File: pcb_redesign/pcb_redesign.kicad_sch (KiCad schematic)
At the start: 6 parts, among them U1 ESP32-S3-WROOM-1

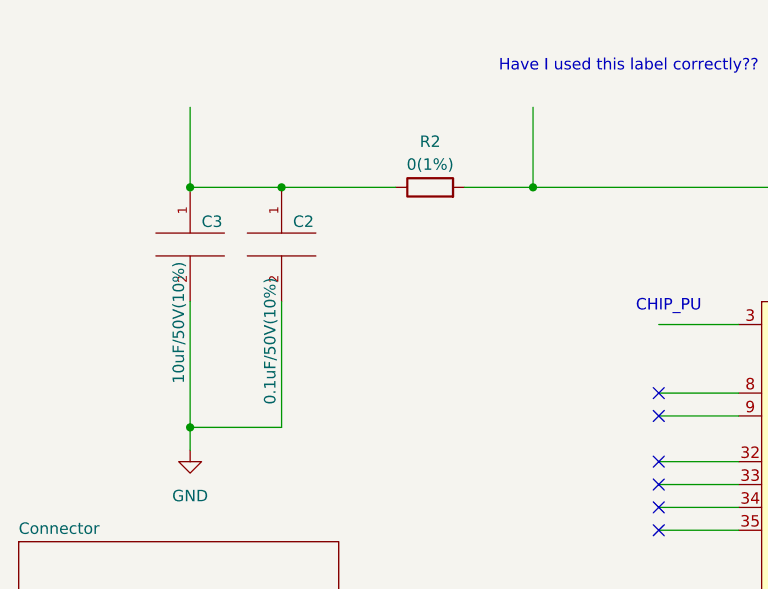
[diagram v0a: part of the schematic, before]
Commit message: schematic imported
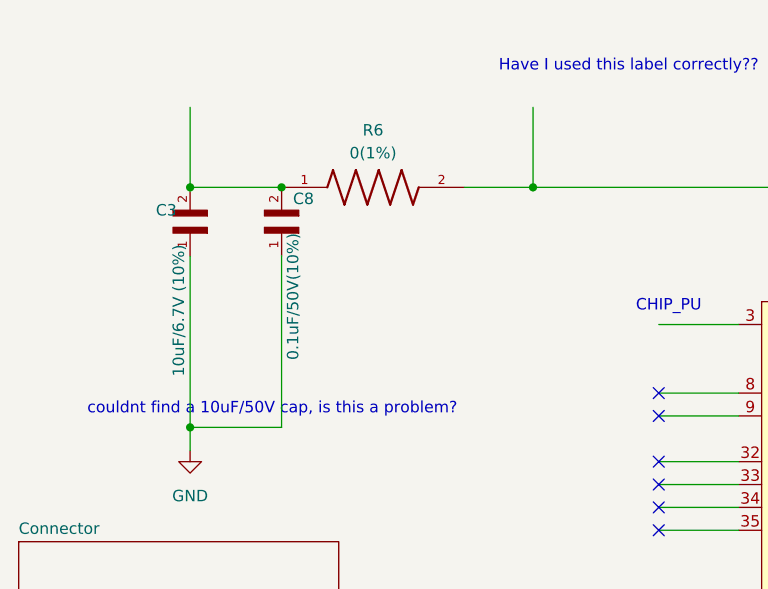
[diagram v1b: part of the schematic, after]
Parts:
- removed C2: 0.1uF/50V(10%), symbol pspice:C
- removed C3: 10uF/50V(10%), 10uF_cap_0805:CAPC2012X140N, symbol pspice:C
- removed R2: 0(1%), symbol Device:R
- added C3: 10uF/6.7V (10%), CAPC1608X90N, symbol 10uf_cap_0603:CL10A106MQ8NNNC
- added C8: 0.1uF/50V(10%), 1uF_cap_0603:CL10A105KB8NNNC, symbol 0.1uF_cap_0603:CL10B104KB8NNNL
- added R6: 0(1%), RESC1508X55N, symbol 0_ohm_0603:RMCF0603ZT0R00
- C1: footprint (none) -> 1uF_cap_0603:CL10A105KB8NNNC
- R1: footprint (none) -> 10k_ohm_0603:RESC1508X50N
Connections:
- net GND: now also C3.1, C8.1
- net at U1.2 (3V3): now also R6.2
- new net: C3.2, C8.2, R6.1
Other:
- note added: "couldnt find a 10uF/50V cap, is this a problem?"
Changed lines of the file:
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@@
 (kicad_sch (version 20230121) (generator eeschema)
   (paper "A4")
+  (junction (at 46.99 43.18) (diameter 0) (color 0 0 0 0)
+  )
   (junction (at 36.83 43.18) (diameter 0) (color 0 0 0 0)
   )
   (junction (at 36.83 69.85) (diameter 0) (color 0 0 0 0)
-  )
-  (junction (at 46.99 43.18) (diameter 0) (color 0 0 0 0)
   )
   (junction (at 66.04 175.26) (diameter 0) (color 0 0 0 0)
@@
     (stroke (width 0) (type default))
   )
+  (wire (pts (xy 88.9 129.54) (xy 97.79 129.54))
+    (stroke (width 0) (type default))
+  )
+  (wire (pts (xy 88.9 81.28) (xy 97.79 81.28))
+    (stroke (width 0) (type default))
+  )
+  (wire (pts (xy 88.9 68.58) (xy 97.79 68.58))
+    (stroke (width 0) (type default))
+  )
+  (wire (pts (xy 36.83 69.85) (xy 46.99 69.85))
+    (stroke (width 0) (type default))
+  )
+  (wire (pts (xy 189.23 129.54) (xy 199.39 129.54))
+    (stroke (width 0) (type default))
+  )
+  (wire (pts (xy 189.23 119.38) (xy 199.39 119.38))
+    (stroke (width 0) (type default))
+  )
   (wire (pts (xy 36.83 43.18) (xy 46.99 43.18))
     (stroke (width 0) (type default))
   )
-  (wire (pts (xy 88.9 129.54) (xy 97.79 129.54))
-    (stroke (width 0) (type default))
-  )
-  (wire (pts (xy 88.9 81.28) (xy 97.79 81.28))
-    (stroke (width 0) (type default))
-  )
-  (wire (pts (xy 88.9 68.58) (xy 97.79 68.58))
-    (stroke (width 0) (type default))
-  )
-  (wire (pts (xy 36.83 69.85) (xy 46.99 69.85))
-    (stroke (width 0) (type default))
-  )
-  (wire (pts (xy 189.23 129.54) (xy 199.39 129.54))
-    (stroke (width 0) (type default))
-  )
-  (wire (pts (xy 189.23 119.38) (xy 199.39 119.38))
-    (stroke (width 0) (type default))
-  )
   (wire (pts (xy 189.23 99.06) (xy 199.39 99.06))
     (stroke (width 0) (type default))
@@
     (stroke (width 0) (type default))
   )
-  (wire (pts (xy 46.99 43.18) (xy 59.69 43.18))
-    (stroke (width 0) (type default))
-  )
   (wire (pts (xy 36.83 69.85) (xy 36.83 72.39))
     (stroke (width 0) (type default))
@@
     (stroke (width 0) (type default))
   )
-  (wire (pts (xy 36.83 55.88) (xy 36.83 69.85))
+  (wire (pts (xy 36.83 50.8) (xy 36.83 69.85))
     (stroke (width 0) (type default))
   )
@@
     (stroke (width 0) (type default))
   )
-  (wire (pts (xy 46.99 55.88) (xy 46.99 69.85))
+  (wire (pts (xy 46.99 50.8) (xy 46.99 69.85))
     (stroke (width 0) (type default))
   )
@@
   )
   (text "Have I used this label correctly??" (at 71.12 30.48 0)
+    (effects (font (size 1.27 1.27)) (justify left bottom))
+  )
+  (text "couldnt find a 10uF/50V cap, is this a problem?" (at 25.4 68.58 0)
     (effects (font (size 1.27 1.27)) (justify left bottom))
   )
@@
       (effects (font (size 1.27 1.27)) (justify left))
     )
-    (property "Footprint" "" (at 64.262 168.91 90)
+    (property "Footprint" "10k_ohm_0603:RESC1508X50N" (at 64.262 168.91 90)
       (effects (font (size 1.27 1.27)) hide)
     )
@@
     )
   )
-  (symbol (lib_id "pspice:C") (at 46.99 49.53 0) (unit 1)
+  (symbol (lib_id "10uf_cap_0603:CL10A106MQ8NNNC") (at 36.83 48.26 90) (unit 1)
     (in_bom yes) (on_board yes) (dnp no)
-    (property "Reference" "C2" (at 48.26 46.99 0)
-      (effects (font (size 1.27 1.27)) (justify left))
-    )
-    (property "Value" "0.1uF/50V(10%)" (at 45.72 67.31 90)
-      (effects (font (size 1.27 1.27)) (justify left))
-    )
-    (property "Footprint" "" (at 46.99 49.53 0)
-      (effects (font (size 1.27 1.27)) hide)
-    )
-    (property "Datasheet" "~" (at 46.99 49.53 0)
+    (property "Reference" "C3" (at 33.02 45.72 90)
+      (effects (font (size 1.27 1.27)) (justify right))
+    )
+    (property "Value" "10uF/6.7V (10%)" (at 35.56 49.53 0)
+      (effects (font (size 1.27 1.27)) (justify right))
+    )
+    (property "Footprint" "CAPC1608X90N" (at 36.83 48.26 0)
+      (effects (font (size 1.27 1.27)) (justify bottom) hide)
+    )
+    (property "Datasheet" "" (at 36.83 48.26 0)
       (effects (font (size 1.27 1.27)) hide)
     )
@@
       (project "pcb_redesign"
         (path "/fb030e39-7dd3-46a0-8379-c26b3ef1b0a0"
-          (reference "C2") (unit 1)
-        )
-      )
-    )
-  )
-  (symbol (lib_id "Device:R") (at 63.5 43.18 90) (unit 1)
-    (in_bom yes) (on_board yes) (dnp no) (fields_autoplaced)
-    (property "Reference" "R2" (at 63.5 38.1 90)
-      (effects (font (size 1.27 1.27)))
-    )
-    (property "Value" "0(1%)" (at 63.5 40.64 90)
-      (effects (font (size 1.27 1.27)))
-    )
-    (property "Footprint" "" (at 63.5 44.958 90)
-      (effects (font (size 1.27 1.27)) hide)
-    )
-    (property "Datasheet" "~" (at 63.5 43.18 0)
+          (reference "C3") (unit 1)
+        )
+      )
+    )
+  )
+  (symbol (lib_id "0.1uF_cap_0603:CL10B104KB8NNNL") (at 46.99 48.26 90) (unit 1)
+    (in_bom yes) (on_board yes) (dnp no)
+    (property "Reference" "C8" (at 48.26 44.45 90)
+      (effects (font (size 1.27 1.27)) (justify right))
+    )
+    (property "Value" "0.1uF/50V(10%)" (at 48.26 48.26 0)
+      (effects (font (size 1.27 1.27)) (justify right))
+    )
+    (property "Footprint" "1uF_cap_0603:CL10A105KB8NNNC" (at 46.99 48.26 0)
+      (effects (font (size 1.27 1.27)) (justify bottom) hide)
+    )
+    (property "Datasheet" "" (at 46.99 48.26 0)
       (effects (font (size 1.27 1.27)) hide)
     )
@@
       (project "pcb_redesign"
         (path "/fb030e39-7dd3-46a0-8379-c26b3ef1b0a0"
-          (reference "R2") (unit 1)
+          (reference "C8") (unit 1)
         )
       )
@@
         (path "/fb030e39-7dd3-46a0-8379-c26b3ef1b0a0"
           (reference "#PWR01") (unit 1)
-        )
-      )
-    )
-  )
-  (symbol (lib_id "pspice:C") (at 36.83 49.53 0) (unit 1)
-    (in_bom yes) (on_board yes) (dnp no)
-    (property "Reference" "C3" (at 38.1 46.99 0)
-      (effects (font (size 1.27 1.27)) (justify left))
-    )
-    (property "Value" "10uF/50V(10%)" (at 35.56 51.435 90)
-      (effects (font (size 1.27 1.27)) (justify right))
-    )
-    (property "Footprint" "10uF_cap_0805:CAPC2012X140N" (at 36.83 49.53 0)
-      (effects (font (size 1.27 1.27)) hide)
-    )
-    (property "Datasheet" "~" (at 36.83 49.53 0)
-      (effects (font (size 1.27 1.27)) hide)
-    )
-    (pin "1")
-    (pin "2")
-    (instances
-      (project "pcb_redesign"
-        (path "/fb030e39-7dd3-46a0-8379-c26b3ef1b0a0"
-          (reference "C3") (unit 1)
         )
       )
@@
       (effects (font (size 1.27 1.27)) (justify left))
     )
-    (property "Footprint" "" (at 66.04 184.15 0)
+    (property "Footprint" "1uF_cap_0603:CL10A105KB8NNNC" (at 66.04 184.15 0)
       (effects (font (size 1.27 1.27)) hide)
     )
@@
         )
       )
+    )
+  )
+  (symbol (lib_id "0_ohm_0603:RMCF0603ZT0R00") (at 57.15 43.18 0) (unit 1)
+    (in_bom yes) (on_board yes) (dnp no) (fields_autoplaced)
+    (property "Reference" "R6" (at 57.15 36.83 0)
+      (effects (font (size 1.27 1.27)))
+    )
+    (property "Value" "0(1%)" (at 57.15 39.37 0)
+      (effects (font (size 1.27 1.27)))
+    )
+    (property "Footprint" "RESC1508X55N" (at 57.15 43.18 0)
+      (effects (font (size 1.27 1.27)) (justify bottom) hide)
+    )
+    (property "Datasheet" "" (at 57.15 43.18 0)
+      (effects (font (size 1.27 1.27)) hide)
+    )
+    (pin "1")
+    (pin "2")
+    (instances
+      (project "pcb_redesign"
+        (path "/fb030e39-7dd3-46a0-8379-c26b3ef1b0a0"
+          (reference "R6") (unit 1)
+        )
+      )

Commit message: components added to board
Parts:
- added JP1: SolderJumper_2_Open, Jumper:SolderJumper-2_P1.3mm_Open_Pad1.0x1.5mm, symbol Jumper:SolderJumper_2_Open
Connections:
- net ESP32_3V3: now reaches R1.1
- net ESP32_3V3: now also R6.2, U1.2 (3V3)
- net CHIP_PU: now reaches C1.1, R1.2
- net CHIP_PU: now also U1.3 (EN)
- net VCC_3V3: now reaches C3.2, C8.2, R6.1
- net at U1.10 (GPIO17/U1TXD/ADC2_CH6): now also JP1.2 (B)
- net at U1.11 (GPIO18/U1RXD/ADC2_CH7/CLK_OUT3): now also JP1.1 (A)
- no-connect marks 30 -> 28
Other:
- note removed: "CHIP_PU"
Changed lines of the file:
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@@
   (no_connect (at 88.9 81.28))
   (no_connect (at 199.39 124.46))
-  (no_connect (at 199.39 114.3))
-  (no_connect (at 199.39 111.76))
   (no_connect (at 199.39 106.68))
   (no_connect (at 199.39 58.42))
@@
     (stroke (width 0) (type default))
   )
+  (wire (pts (xy 203.2 114.3) (xy 203.2 116.84))
+    (stroke (width 0) (type default))
+  )
   (wire (pts (xy 36.83 69.85) (xy 36.83 72.39))
     (stroke (width 0) (type default))
   )
-  (wire (pts (xy 189.23 114.3) (xy 199.39 114.3))
+  (wire (pts (xy 189.23 114.3) (xy 203.2 114.3))
     (stroke (width 0) (type default))
   )
@@
     (stroke (width 0) (type default))
   )
+  (wire (pts (xy 189.23 111.76) (xy 203.2 111.76))
+    (stroke (width 0) (type default))
+  )
   (wire (pts (xy 67.31 43.18) (xy 74.93 43.18))
     (stroke (width 0) (type default))
@@
     (stroke (width 0) (type default))
   )
-  (wire (pts (xy 189.23 111.76) (xy 199.39 111.76))
+  (wire (pts (xy 203.2 111.76) (xy 203.2 109.22))
     (stroke (width 0) (type default))
   )
@@
     (stroke (width 0) (type default))
   )
+  (wire (pts (xy 203.2 116.84) (xy 207.01 116.84))
+    (stroke (width 0) (type default))
+  )
   (wire (pts (xy 189.23 104.14) (xy 199.39 104.14))
     (stroke (width 0) (type default))
@@
     (stroke (width 0) (type default))
   )
+  (wire (pts (xy 203.2 109.22) (xy 207.01 109.22))
+    (stroke (width 0) (type default))
+  )
   (wire (pts (xy 189.23 81.28) (xy 199.39 81.28))
     (stroke (width 0) (type default))
@@
     (stroke (width 0) (type default))
   )
-  (text "Goes to pad (and then gnd..?)" (at 208.28 115.57 0)
+  (text "Goes to pad (and then gnd..?)" (at 232.41 106.68 0)
     (effects (font (size 1.27 1.27)) (justify left bottom))
   )
@@
     (effects (font (size 1.27 1.27)) (justify left bottom))
   )
-  (text "Goes to pad (and then gnd..?)" (at 208.28 113.03 0)
+  (text "Goes to pad (and then gnd..?)" (at 232.41 104.14 0)
     (effects (font (size 1.27 1.27)) (justify left bottom))
   )
@@
     (effects (font (size 1.27 1.27)) (justify left bottom))
   )
-  (text "CHIP_PU" (at 74.93 175.26 0)
-    (effects (font (size 1.27 1.27)) (justify left bottom))
-  )
   (text "If I dont want a pin to be accessible, do I ground the pin or do I mark it as not connected\nAnswer: mark as nc"
     (at 193.04 50.8 0)
     (effects (font (size 1.27 1.27)) (justify left bottom))
   )
-  (text "CHIP_PU" (at 86.36 57.15 0)
-    (effects (font (size 1.27 1.27)) (justify left bottom))
+  (label "CHIP_PU" (at 78.74 175.26 0) (fields_autoplaced)
+    (effects (font (size 1.27 1.27)) (justify left bottom))
+  )
+  (label "CHIP_PU" (at 88.9 58.42 0) (fields_autoplaced)
+    (effects (font (size 1.27 1.27)) (justify left bottom))
+  )
+  (label "ESP32_3V3" (at 66.04 165.1 0) (fields_autoplaced)
+    (effects (font (size 1.27 1.27)) (justify left bottom))
+  )
+  (label "ESP32_3V3" (at 74.93 34.29 0) (fields_autoplaced)
+    (effects (font (size 1.27 1.27)) (justify left bottom))
+  )
+  (global_label "GND" (shape output) (at 143.51 134.62 270) (fields_autoplaced)
+    (effects (font (size 1.27 1.27)) (justify right))
+    (property "Intersheetrefs" "${INTERSHEET_REFS}" (at 143.51 141.3963 90)
+      (effects (font (size 1.27 1.27)) (justify right) hide)
+    )
   )
   (global_label "ENB Left Motor" (shape output) (at 199.39 86.36 0) (fields_autoplaced)
@@
     )
   )
+  (global_label "VCC_3V3" (shape input) (at 36.83 34.29 90) (fields_autoplaced)
+    (effects (font (size 1.27 1.27)) (justify left))
+    (property "Intersheetrefs" "${INTERSHEET_REFS}" (at 36.83 23.2804 90)
+      (effects (font (size 1.27 1.27)) (justify left) hide)
+    )
+  )
   (global_label "D-" (shape input) (at 199.39 68.58 0) (fields_autoplaced)
     (effects (font (size 1.27 1.27)) (justify left))
@@
     )
   )
+  (global_label "GND" (shape output) (at 66.04 190.5 270) (fields_autoplaced)
+    (effects (font (size 1.27 1.27)) (justify right))
+    (property "Intersheetrefs" "${INTERSHEET_REFS}" (at 66.04 197.2763 90)
+      (effects (font (size 1.27 1.27)) (justify right) hide)
+    )
+  )
+  (global_label "GND" (shape output) (at 36.83 72.39 270) (fields_autoplaced)
+    (effects (font (size 1.27 1.27)) (justify right))
+    (property "Intersheetrefs" "${INTERSHEET_REFS}" (at 36.83 79.1663 90)
+      (effects (font (size 1.27 1.27)) (justify right) hide)
+    )
+  )
   (global_label "D+" (shape input) (at 199.39 66.04 0) (fields_autoplaced)
     (effects (font (size 1.27 1.27)) (justify left))
     (property "Intersheetrefs" "${INTERSHEET_REFS}" (at 205.1382 66.04 0)
       (effects (font (size 1.27 1.27)) (justify left) hide)
-    )
-  )
-  (netclass_flag "" (length 2.54) (shape round) (at 66.04 165.1 0) (fields_autoplaced)
-    (effects (font (size 1.27 1.27)) (justify left bottom))
-    (property "Netclass" "ESP32_3V3" (at 66.7385 162.56 0)
-      (effects (font (size 1.27 1.27) italic) (justify left))
-    )
-  )
-  (netclass_flag "" (length 2.54) (shape round) (at 36.83 34.29 0) (fields_autoplaced)
-    (effects (font (size 1.27 1.27)) (justify left bottom))
-    (property "Netclass" "VCC_3V3" (at 37.5285 31.75 0)
-      (effects (font (size 1.27 1.27) italic) (justify left))
-    )
-  )
-  (netclass_flag "" (length 2.54) (shape round) (at 74.93 34.29 0) (fields_autoplaced)
-    (effects (font (size 1.27 1.27)) (justify left bottom))
-    (property "Netclass" "ESP32_3V3" (at 75.6285 31.75 0)
-      (effects (font (size 1.27 1.27) italic) (justify left))
     )
   )
@@
         (path "/fb030e39-7dd3-46a0-8379-c26b3ef1b0a0"
           (reference "C8") (unit 1)
-        )
-      )
-    )
-  )
-  (symbol (lib_id "power:GND") (at 143.51 134.62 0) (unit 1)
-    (in_bom yes) (on_board yes) (dnp no) (fields_autoplaced)
-    (property "Reference" "#PWR01" (at 143.51 140.97 0)
-      (effects (font (size 1.27 1.27)) hide)
-    )
-    (property "Value" "GND" (at 143.51 139.7 0)
-      (effects (font (size 1.27 1.27)))
-    )
-    (property "Footprint" "" (at 143.51 134.62 0)
-      (effects (font (size 1.27 1.27)) hide)
-    )
-    (property "Datasheet" "" (at 143.51 134.62 0)
-      (effects (font (size 1.27 1.27)) hide)
-    )
-    (pin "1")
-    (instances
-      (project "pcb_redesign"
-        (path "/fb030e39-7dd3-46a0-8379-c26b3ef1b0a0"
-          (reference "#PWR01") (unit 1)
-        )
-      )
-    )
-  )
-  (symbol (lib_id "power:GND") (at 66.04 190.5 0) (unit 1)
-    (in_bom yes) (on_board yes) (dnp no) (fields_autoplaced)
-    (property "Reference" "#PWR02" (at 66.04 196.85 0)
-      (effects (font (size 1.27 1.27)) hide)
-    )
-    (property "Value" "GND" (at 66.04 195.58 0)
-      (effects (font (size 1.27 1.27)))
-    )
-    (property "Footprint" "" (at 66.04 190.5 0)
-      (effects (font (size 1.27 1.27)) hide)
-    )
-    (property "Datasheet" "" (at 66.04 190.5 0)
-      (effects (font (size 1.27 1.27)) hide)
-    )
-    (pin "1")
-    (instances
-      (project "pcb_redesign"
-        (path "/fb030e39-7dd3-46a0-8379-c26b3ef1b0a0"
-          (reference "#PWR02") (unit 1)
         )
       )
@@
     )
   )
-  (symbol (lib_id "power:GND") (at 36.83 72.39 0) (unit 1)
+  (symbol (lib_id "Jumper:SolderJumper_2_Open") (at 207.01 113.03 90) (unit 1)
     (in_bom yes) (on_board yes) (dnp no) (fields_autoplaced)
-    (property "Reference" "#PWR03" (at 36.83 78.74 0)
-      (effects (font (size 1.27 1.27)) hide)
-    )
-    (property "Value" "GND" (at 36.83 77.47 0)
-      (effects (font (size 1.27 1.27)))
-    )
-    (property "Footprint" "" (at 36.83 72.39 0)
-      (effects (font (size 1.27 1.27)) hide)
-    )
-    (property "Datasheet" "" (at 36.83 72.39 0)
-      (effects (font (size 1.27 1.27)) hide)
-    )
-    (pin "1")
-    (instances
-      (project "pcb_redesign"
-        (path "/fb030e39-7dd3-46a0-8379-c26b3ef1b0a0"
-          (reference "#PWR03") (unit 1)
+    (property "Reference" "JP1" (at 209.55 112.395 90)
+      (effects (font (size 1.27 1.27)) (justify right))
+    )
+    (property "Value" "SolderJumper_2_Open" (at 209.55 114.935 90)
+      (effects (font (size 1.27 1.27)) (justify right))
+    )
+    (property "Footprint" "Jumper:SolderJumper-2_P1.3mm_Open_Pad1.0x1.5mm" (at 207.01 113.03 0)
+      (effects (font (size 1.27 1.27)) hide)
+    )
+    (property "Datasheet" "~" (at 207.01 113.03 0)
+      (effects (font (size 1.27 1.27)) hide)
+    )
+    (pin "1")
+    (pin "2")
+    (instances
+      (project "pcb_redesign"
+        (path "/fb030e39-7dd3-46a0-8379-c26b3ef1b0a0"
+          (reference "JP1") (unit 1)
         )
       )
@@
     (instances
       (project "pcb_redesign"
-        (path "/fb030e39-7dd3-46a0-8379-c26b3ef1b0a0" (page "4"))
-      )
-    )
+        (path "/fb030e39-7dd3-46a0-8379-c26b3ef1b0a0" (page "3"))
+      )
+    )

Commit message: switching to laptop
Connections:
- net ENA Left Motor: now also U1.39 (GPIO1/TOUCH1/ADC1_CH0); no longer U1.4 (GPIO4/TOUCH4/ADC1_CH3)
- net ENA Right Motor: now also U1.5 (GPIO5/TOUCH5/ADC1_CH4); no longer U1.39 (GPIO1/TOUCH1/ADC1_CH0)
- net ENB Left Motor: now also U1.38 (GPIO2/TOUCH2/ADC1_CH1); no longer U1.5 (GPIO5/TOUCH5/ADC1_CH4)
- net ENB Right Motor: now also U1.4 (GPIO4/TOUCH4/ADC1_CH3); no longer U1.38 (GPIO2/TOUCH2/ADC1_CH1)
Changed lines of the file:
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@@
     )
   )
-  (global_label "ENB Left Motor" (shape output) (at 199.39 86.36 0) (fields_autoplaced)
+  (global_label "ENA Right Motor" (shape output) (at 199.39 86.36 0) (fields_autoplaced)
     (effects (font (size 1.27 1.27)) (justify left))
-    (property "Intersheetrefs" "${INTERSHEET_REFS}" (at 216.8099 86.36 0)
+    (property "Intersheetrefs" "${INTERSHEET_REFS}" (at 217.9589 86.36 0)
       (effects (font (size 1.27 1.27)) (justify left) hide)
     )
   )
-  (global_label "ENA Left Motor" (shape output) (at 199.39 83.82 0) (fields_autoplaced)
+  (global_label "ENA Left Motor" (shape output) (at 199.39 76.2 0) (fields_autoplaced)
     (effects (font (size 1.27 1.27)) (justify left))
-    (property "Intersheetrefs" "${INTERSHEET_REFS}" (at 216.6285 83.82 0)
+    (property "Intersheetrefs" "${INTERSHEET_REFS}" (at 216.6285 76.2 0)
       (effects (font (size 1.27 1.27)) (justify left) hide)
     )
@@
     )
   )
+  (global_label "ENB Right Motor" (shape output) (at 199.39 83.82 0) (fields_autoplaced)
+    (effects (font (size 1.27 1.27)) (justify left))
+    (property "Intersheetrefs" "${INTERSHEET_REFS}" (at 218.1403 83.82 0)
+      (effects (font (size 1.27 1.27)) (justify left) hide)
+    )
+  )
   (global_label "D-" (shape input) (at 199.39 68.58 0) (fields_autoplaced)
     (effects (font (size 1.27 1.27)) (justify left))
     (property "Intersheetrefs" "${INTERSHEET_REFS}" (at 205.1382 68.58 0)
-      (effects (font (size 1.27 1.27)) (justify left) hide)
-    )
-  )
-  (global_label "ENA Right Motor" (shape output) (at 199.39 76.2 0) (fields_autoplaced)
-    (effects (font (size 1.27 1.27)) (justify left))
-    (property "Intersheetrefs" "${INTERSHEET_REFS}" (at 217.9589 76.2 0)
-      (effects (font (size 1.27 1.27)) (justify left) hide)
-    )
-  )
-  (global_label "ENB Right Motor" (shape output) (at 199.39 78.74 0) (fields_autoplaced)
-    (effects (font (size 1.27 1.27)) (justify left))
-    (property "Intersheetrefs" "${INTERSHEET_REFS}" (at 218.1403 78.74 0)
       (effects (font (size 1.27 1.27)) (justify left) hide)
     )
@@
     )
   )
+  (global_label "ENB Left Motor" (shape output) (at 199.39 78.74 0) (fields_autoplaced)
+    (effects (font (size 1.27 1.27)) (justify left))
+    (property "Intersheetrefs" "${INTERSHEET_REFS}" (at 216.8099 78.74 0)
+      (effects (font (size 1.27 1.27)) (justify left) hide)
+    )
+  )
